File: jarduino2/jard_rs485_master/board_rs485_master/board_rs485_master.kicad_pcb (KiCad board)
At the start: 2 copper layers, 132.4 x 70.8 mm, 64 parts, among them J1 POWER_12V, J2 Log, J3 POWER_OYAS_12V, J4 BUS_OYAS, J5 Leds RGB, J6 Button, J7 Adapt BUS, Q1 BPC_2N2222A, Q2 P03P4L-04, Q3 BC327, Q4 BC327, Q5 BPC_2N2222A, Q6 BPC_2N2222A, U1 RtcArduino, U2 BPC_Alim5V, U3 BPC_ESP8266-01_ESP-01, U4 BPC_Mod485, U5 LM1117DT-3.3

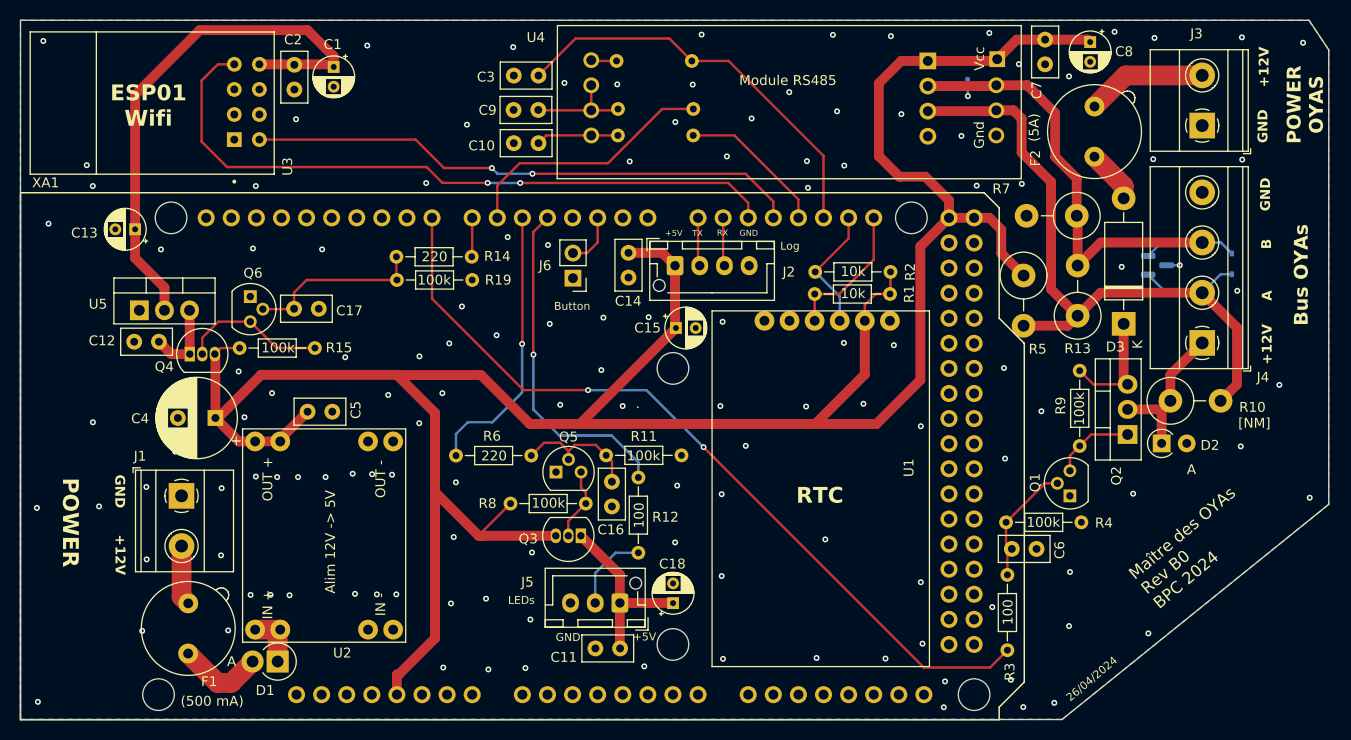
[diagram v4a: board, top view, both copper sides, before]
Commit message: Réaffactation des commandes PWR de Wifi et LEDs (compatibilité soft) + suppression de la sheet Wifi sur le schéma (regreoupé dans UC)
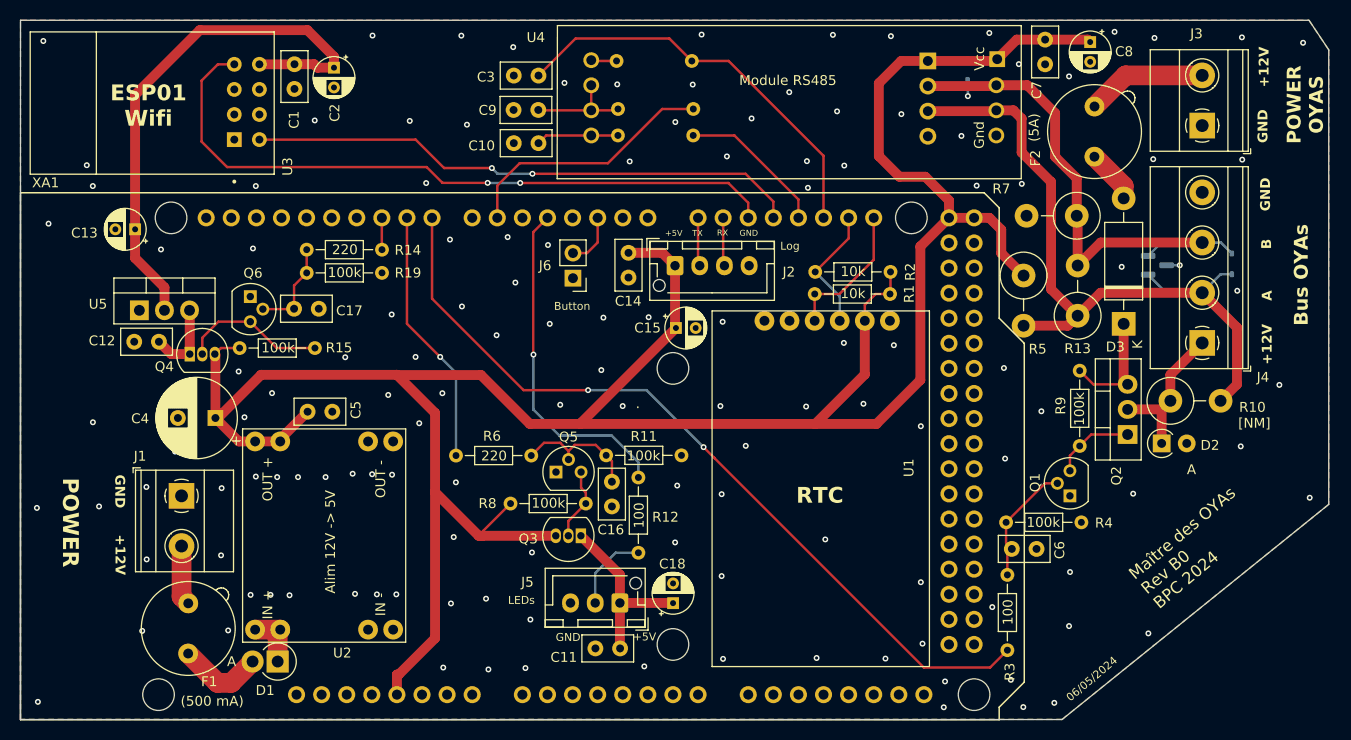
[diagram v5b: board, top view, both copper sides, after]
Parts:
- C1: value 10µF -> 100nF; footprint Capacitor_THT:CP_Radial_D4.0mm_P2.00mm -> Capacitor_THT:C_Disc_D5.0mm_W2.5mm_P2.50mm
- C2: value 100nF -> 10µF; footprint Capacitor_THT:C_Disc_D5.0mm_W2.5mm_P2.50mm -> Capacitor_THT:CP_Radial_D4.0mm_P2.00mm
- moved R19 9.16 mm to (103.5, 74.6)
- moved R14 9.11 mm to (111.2, 72.2)
- moved C2 4.02 mm to (106.3, 53.8)
- moved C1 3.98 mm to (102.3, 53.5)
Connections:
- XA1 pad D10: unconnected-(XA1-PadD10) -> CMD_WIFI_PWR
- XA1 pad D5: CMD_LEDS_PWR -> unconnected-(XA1-PadD5)
- XA1 pad D7: CMD_WIFI_PWR -> unconnected-(XA1-PadD7)
- XA1 pad D9: unconnected-(XA1-PadD9) -> CMD_LEDS_PWR
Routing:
- net Net-(C17-Pad1): track 18.1 -> 9.69 mm
- net CMD_LEDS_PWR: track 28.3 -> 26.1 mm
- net CMD_WIFI_PWR: track 3.96 -> 3.23 mm
- net GND: vias 133 -> 136
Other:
- board text added: "06/05/2024"
- board text removed: "26/04/2024"
